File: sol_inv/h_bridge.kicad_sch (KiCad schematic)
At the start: 38 parts, among them J1 Screw_Terminal_01x02, J2 Screw_Terminal_01x02, T1 12uH, 1.7A, T2 12uH, 1.7A, T3 12uH, 1.7A, U1 MCP6001-OT, U11 MCP6001-OT, U2 MCP6001-OT, U3 INA240A1D, U4 INA240A1D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

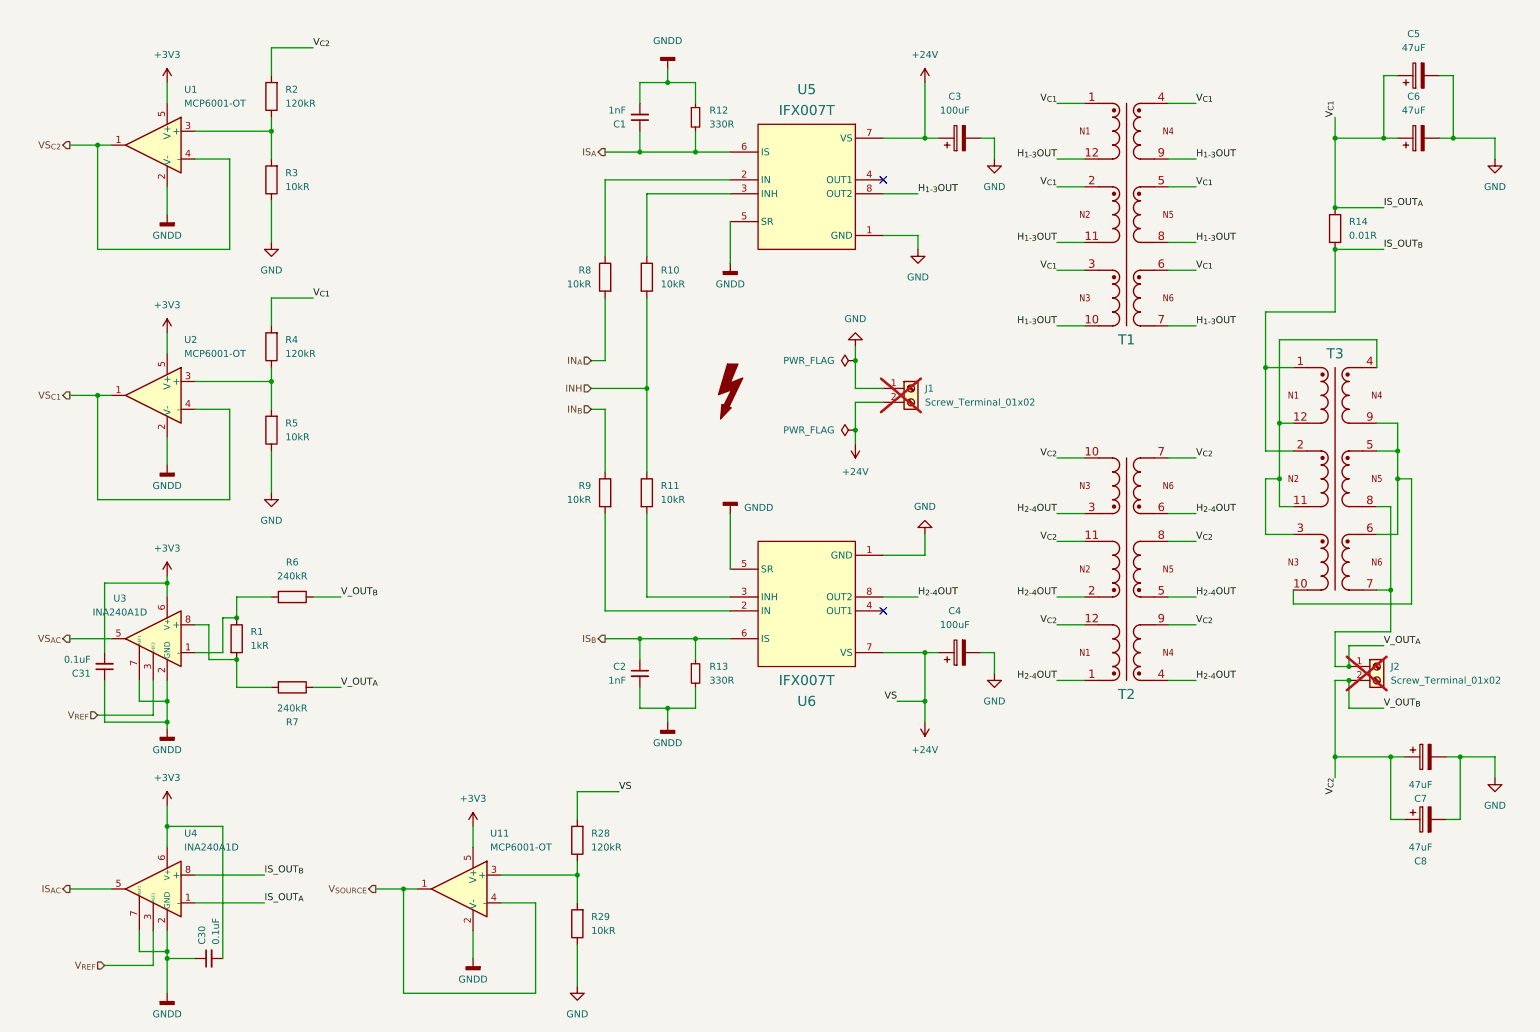
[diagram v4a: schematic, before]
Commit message: v0.3.4 fixes + component change for farnell
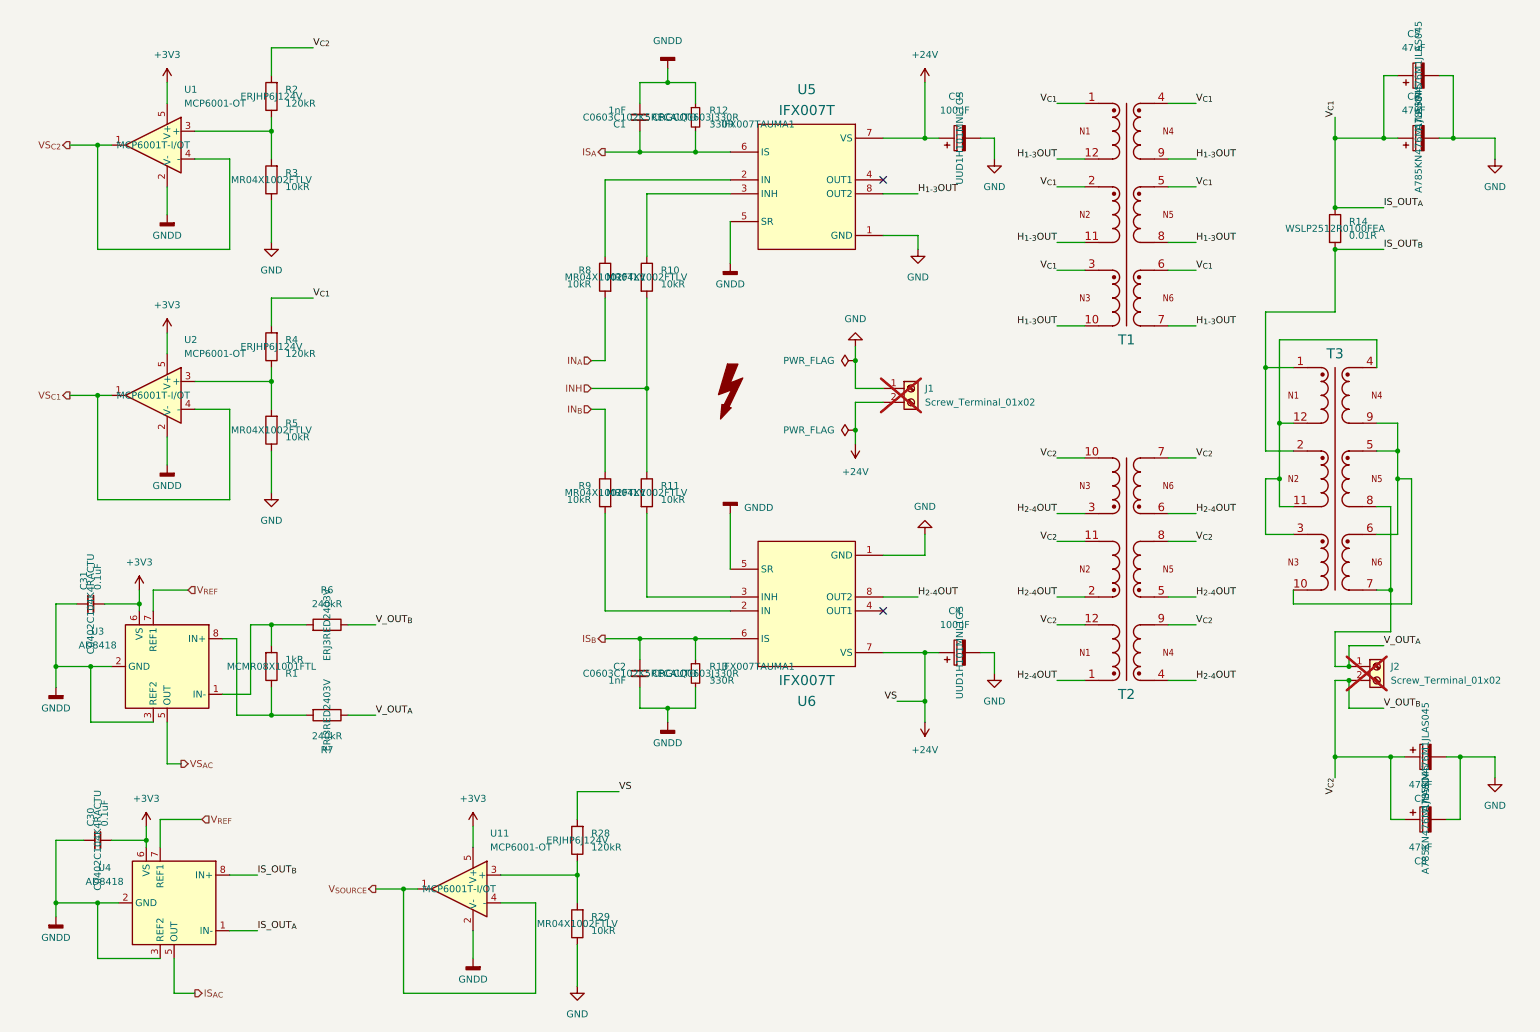
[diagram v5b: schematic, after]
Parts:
- removed U3, U4: INA240A1D, INA240A1D:D8_TEX, symbol Amplifier_Current:INA240A1D
- added U3, U4: AD8418, Package_SO:SOIC-8_3.9x4.9mm_P1.27mm, symbol Amplifier_Current:AD8418
- C1, C2: Manufacturer Part Number (none) -> C0603C102K5RECAUTO
- C3, C4: Manufacturer Part Number (none) -> UUD1H101MNL1GS
- C30, C31: Manufacturer Part Number (none) -> C0402C104K4RACTU
- C5, C6, C7, C8: Manufacturer Part Number (none) -> A785KN476M1JLAS045
- R1: Manufacturer Part Number (none) -> MCMR08X1001FTL
- R10, R11, R29, R3, R5, R8, R9: Manufacturer Part Number (none) -> MR04X1002FTLV
- R12, R13: Manufacturer Part Number (none) -> CRGCQ0603J330R
- R14: Manufacturer Part Number (none) -> WSLP2512R0100FEA
- R2, R28, R4: Manufacturer Part Number (none) -> ERJHP6J124V
- R6, R7: Manufacturer Part Number (none) -> ERJ3RED2403V
- U1, U11, U2: Manufacturer Part Number (none) -> MCP6001T-I/OT
- U5, U6: Manufacturer Part Number (none) -> IFX007TAUMA1
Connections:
- net +3V3: now also U3.6 (VS), U4.6 (VS)
- net GNDD: now also U3.2 (GND), U3.3 (REF2), U4.2 (GND), U4.3 (REF2)
- net IS_OUT_{A}: now also U4.1 (IN-)
- net IS_OUT_{B}: now also U4.8 (IN+)
- net IS_{AC}: now also U4.5 (OUT)
- net VS_{AC}: now also U3.5 (OUT)
- net V_{REF}: now also U3.7 (REF1), U4.7 (REF1)
- net at R1.1: now also R7.2, U3.8 (IN+); no longer R6.2
- net at R1.2: now also R6.2, U3.1 (IN-); no longer R7.2
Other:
- moved on the sheet: C30, C31, R1, R6, R7

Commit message: v0.4 fixed mcu ldo part, production testing
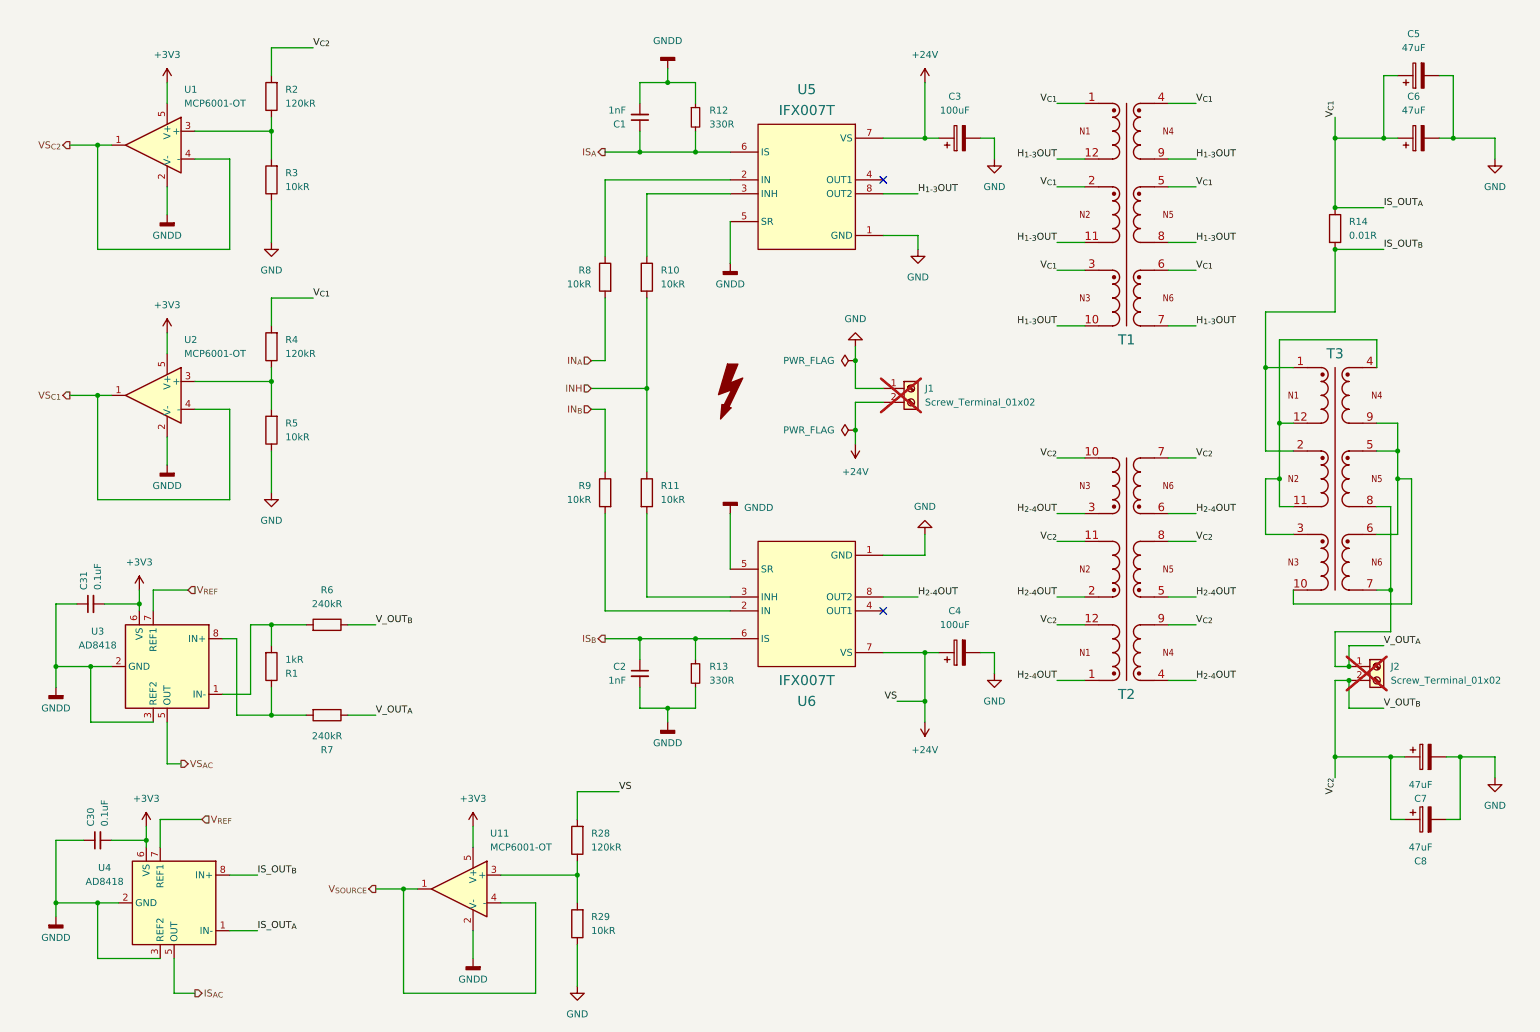
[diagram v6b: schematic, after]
